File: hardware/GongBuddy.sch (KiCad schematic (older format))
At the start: 49 parts, among them J1 USB_B_Mini, J2 Conn_01x05, J3 2908-05WB-MG, J4 Conn_01x04, J5 Conn_01x02, J6 Conn_01x06, J7 Conn_Coaxial, J8 Conn_01x15, Q1 MMBT3904, U1 TPS7A19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

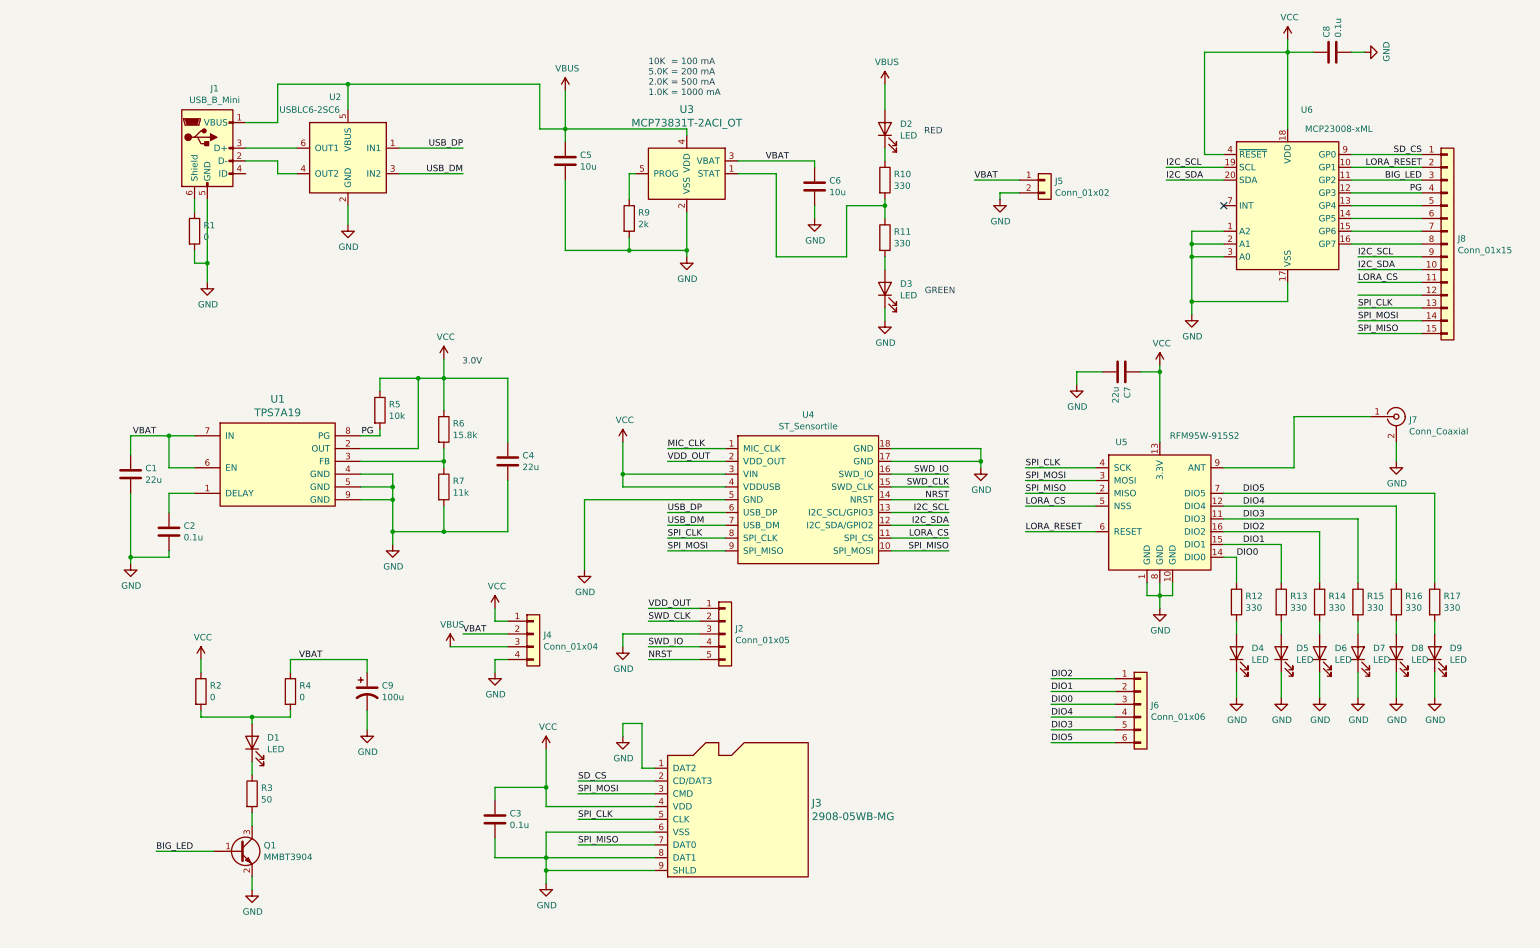
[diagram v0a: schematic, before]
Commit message: Finished the layout and routing.
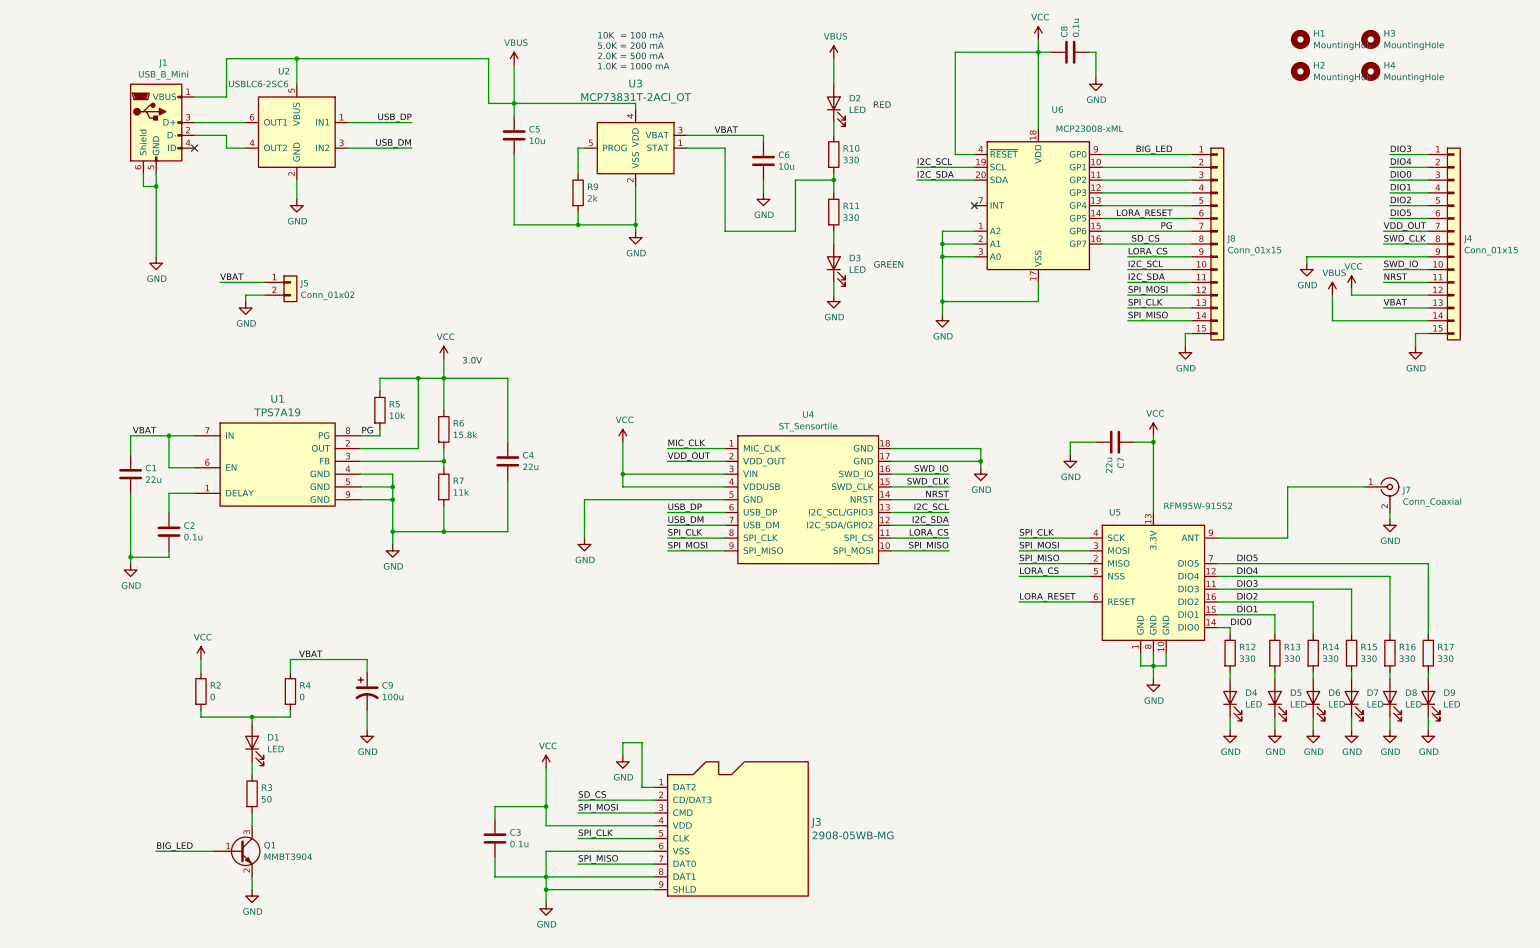
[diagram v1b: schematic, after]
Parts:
- removed J2: Conn_01x05, Connector_PinHeader_2.54mm:PinHeader_1x05_P2.54mm_Vertical, symbol Connector_Generic:Conn_01x05
- removed J4: Conn_01x04, Connector_PinHeader_2.54mm:PinHeader_1x04_P2.54mm_Vertical, symbol Connector_Generic:Conn_01x04
- removed J6: Conn_01x06, Connector_PinHeader_2.54mm:PinHeader_1x06_P2.54mm_Vertical, symbol Connector_Generic:Conn_01x06
- removed R1: 0, Resistor_SMD:R_0603_1608Metric, symbol Device:R
- added H1, H2, H3, H4: MountingHole, MountingHole:MountingHole_2.7mm_M2.5, symbol Mechanical:MountingHole
- added J4: Conn_01x15, Connector_PinHeader_2.54mm:PinHeader_1x15_P2.54mm_Vertical, symbol Connector_Generic:Conn_01x15
- C9: footprint Capacitor_SMD:CP_Elec_6.3x5.7 -> Capacitor_SMD:CP_Elec_3x5.3
- R3: footprint Resistor_SMD:R_0603_1608Metric -> Resistor_SMD:R_1206_3216Metric
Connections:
- net BIG_LED: now also J8.1 (Pin_1), U6.9 (GP0); no longer J8.3 (Pin_3), U6.11 (GP2)
- net DIO0: now also J4.3 (Pin_3)
- net DIO1: now also J4.4 (Pin_4)
- net DIO2: now also J4.5 (Pin_5)
- net DIO3: now also J4.1 (Pin_1)
- net DIO4: now also J4.2 (Pin_2)
- net DIO5: now also J4.6 (Pin_6)
- net GND: now also J1.6 (Shield), J8.15 (Pin_15), J4.15 (Pin_15), J4.9 (Pin_9)
- net I2C_SCL: now also J8.10 (Pin_10); no longer J8.9 (Pin_9)
- net I2C_SDA: now also J8.11 (Pin_11); no longer J8.10 (Pin_10)
- net LORA_CS: now also J8.9 (Pin_9); no longer J8.11 (Pin_11)
- net LORA_RESET: now also J8.6 (Pin_6), U6.14 (GP5); no longer J8.2 (Pin_2), U6.10 (GP1)
- net NRST: now also J4.11 (Pin_11)
- net PG: now also J8.7 (Pin_7), U6.15 (GP6); no longer J8.4 (Pin_4), U6.12 (GP3)
- net SD_CS: now also J8.8 (Pin_8), U6.16 (GP7); no longer J8.1 (Pin_1), U6.9 (GP0)
- net SPI_MISO: now also J8.14 (Pin_14); no longer J8.15 (Pin_15)
- net SPI_MOSI: now also J8.12 (Pin_12); no longer J8.14 (Pin_14)
- net SWD_CLK: now also J4.8 (Pin_8)
- net SWD_IO: now also J4.10 (Pin_10)
- net VBAT: now also J4.13 (Pin_13)
- net VBUS: now also J4.14 (Pin_14)
- net VCC: now also J4.12 (Pin_12)
- net VDD_OUT: now also J4.7 (Pin_7)
- new net: J8.2 (Pin_2), U6.10 (GP1)
- new net: J8.3 (Pin_3), U6.11 (GP2)
- new net: J8.4 (Pin_4), U6.12 (GP3)
- no-connect marks 1 -> 2
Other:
- moved on the sheet: C3, C5, C6, C7, C8, D2, D3, D4, D5, D6, D7, D8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

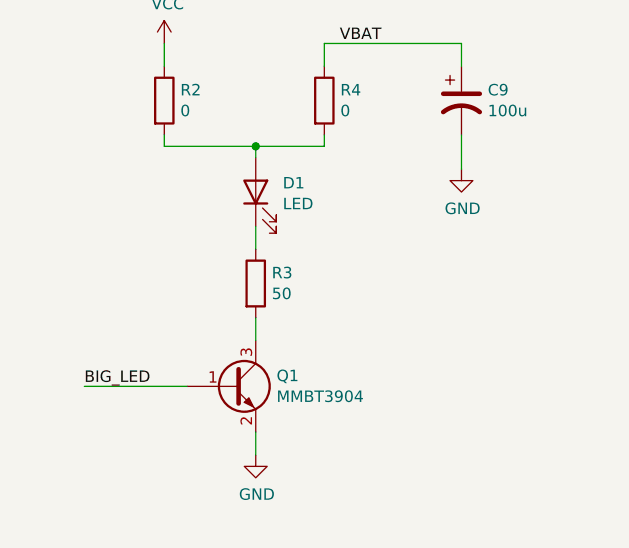
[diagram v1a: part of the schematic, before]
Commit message: Tweaked the layout slightly.
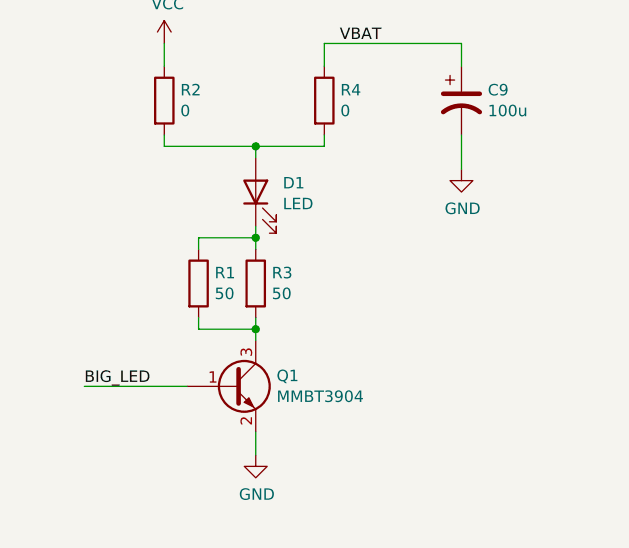
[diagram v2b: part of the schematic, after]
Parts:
- added R1: 50, Resistor_SMD:R_1206_3216Metric, symbol Device:R
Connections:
- net at Q1.3 (C), R3.2: now also R1.2
- net at D1.1 (K), R3.1: now also R1.1
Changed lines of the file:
@@
 VBAT
 Wire Wire Line
-	1600 6400 1600 6500
-Wire Wire Line
-	1600 6800 1600 6900
+	1600 6400 1600 6450
+Wire Wire Line
+	1600 6800 1600 6850
 $Comp
 L power:GND #PWR04
@@
 	850  1900 850  2450
 NoConn ~ 1150 1600
+$Comp
+L Device:R R1
+U 1 1 5F92D8FD
+P 1350 6650
+F 0 "R1" H 1420 6696 50  0000 L CNN
+F 1 "50" H 1420 6605 50  0000 L CNN
+F 2 "Resistor_SMD:R_1206_3216Metric" V 1280 6650 50  0001 C CNN
+F 3 "~" H 1350 6650 50  0001 C CNN
+	1    1350 6650
+	1    0    0    -1
+$EndComp
+Wire Wire Line
+	1350 6500 1350 6450
+Wire Wire Line
+	1350 6450 1600 6450
+Connection ~ 1600 6450
+Wire Wire Line
+	1600 6450 1600 6500
+Wire Wire Line
+	1350 6800 1350 6850
+Wire Wire Line
+	1350 6850 1600 6850
+Connection ~ 1600 6850
+Wire Wire Line
+	1600 6850 1600 6900
 $EndSCHEMATC

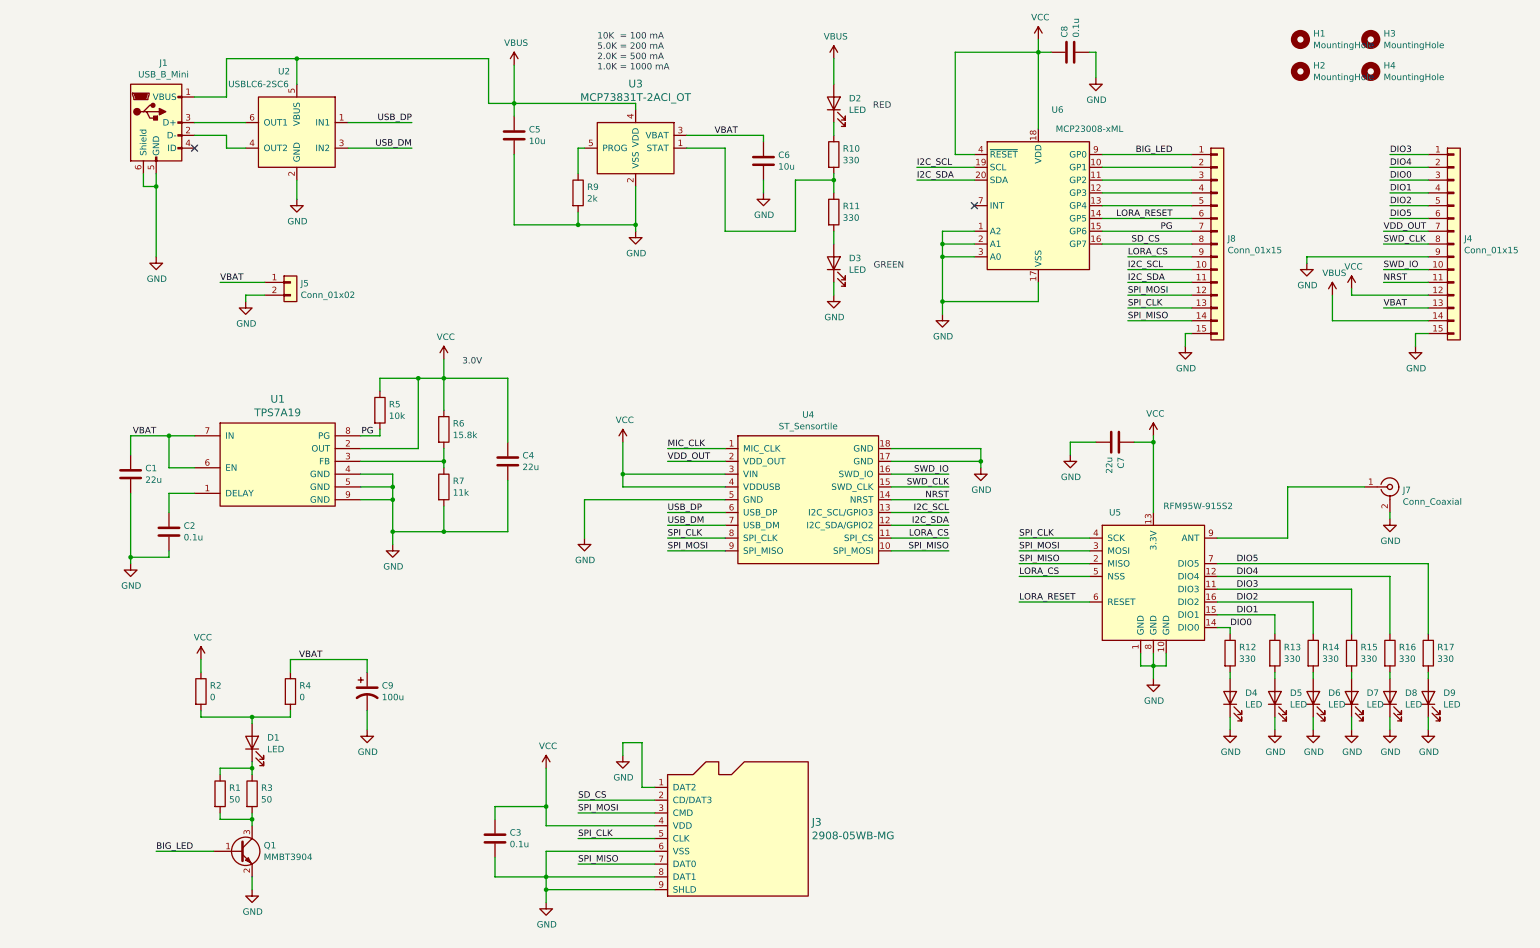
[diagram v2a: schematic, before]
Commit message: Updated the mechanical design, step files, etc.
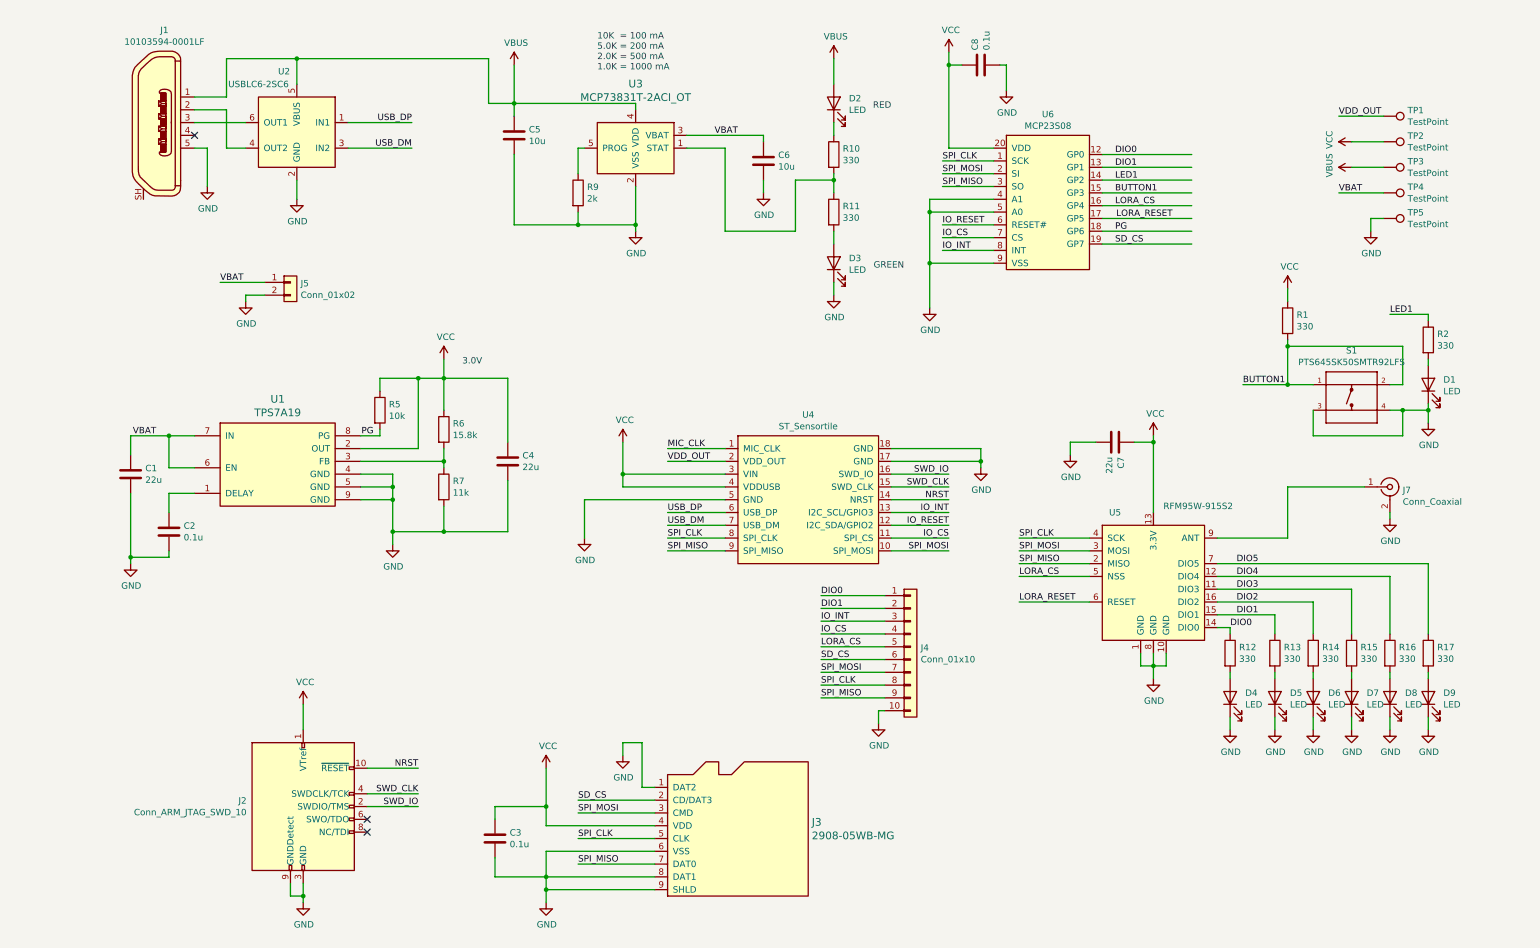
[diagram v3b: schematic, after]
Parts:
- removed C9: 100u, Capacitor_SMD:CP_Elec_3x5.3, symbol Device:CP1
- removed H1, H2, H3, H4: MountingHole, MountingHole:MountingHole_2.7mm_M2.5, symbol Mechanical:MountingHole
- removed J1: USB_B_Mini, Connector_USB:USB_Mini-B_Lumberg_2486_01_Horizontal, symbol Connector:USB_B_Mini
- removed J4, J8: Conn_01x15, Connector_PinHeader_2.54mm:PinHeader_1x15_P2.54mm_Vertical, symbol Connector_Generic:Conn_01x15
- removed Q1: MMBT3904, Package_TO_SOT_SMD:SOT-23, symbol Transistor_BJT:MMBT3904
- removed R3: 50, Resistor_SMD:R_1206_3216Metric, symbol Device:R
- removed R4: 0, Resistor_SMD:R_0603_1608Metric, symbol Device:R
- removed U6: MCP23008-xML, Package_DFN_QFN:QFN-20-1EP_4x4mm_P0.5mm_EP2.7x2.7mm, symbol Interface_Expansion:MCP23008-xML
- added J1: 10103594-0001LF, digikey-footprints:USB_Micro_B_Female_10103594-0001LF, symbol dk_USB-DVI-HDMI-Connectors:10103594-0001LF
- added J2: Conn_ARM_JTAG_SWD_10, KicadFootprint:CortexSWD, symbol Connector:Conn_ARM_JTAG_SWD_10
- added J4: Conn_01x10, Connector_PinHeader_2.54mm:PinHeader_1x10_P2.54mm_Vertical, symbol Connector_Generic:Conn_01x10
- added S1: PTS645SK50SMTR92LFS, mechanical:SW_PTS645SK50SMTR92LFS, symbol PTS645SK50SMTR92LFS:PTS645SK50SMTR92LFS
- added TP1, TP2, TP3, TP4, TP5: TestPoint, TestPoint:TestPoint_Pad_D1.0mm, symbol Connector:TestPoint
- added U6: MCP23S08, Package_SO:SSOP-20_5.3x7.2mm_P0.65mm, symbol General:MCP23S08
- D1: footprint LED_THT:LED_D1.8mm_W1.8mm_H2.4mm_Horizontal_O1.27mm_Z1.6mm -> LED_SMD:LED_0603_1608Metric
- J3: footprint KicadFootprint:AMPHENOL_1140084168 -> digikey-footprints:MicroSD_2908-05WB-MG; Digi-Key_PN 114-00841-68-2-ND -> 3M5607CT-ND; MPN 114-00841-68 -> 2908-05WB-MG
- J7: footprint Connector_Coaxial:SMA_Amphenol_132289_EdgeMount -> KicadFootprint:SAMTEC_SMA-J-P-H-ST-EM1
- R1: value 50 -> 330; footprint Resistor_SMD:R_1206_3216Metric -> Resistor_SMD:R_0603_1608Metric
- R2: value 0 -> 330
- U1: footprint Package_SON:HVSON-8-1EP_3x3mm_P0.65mm_EP1.6x2.4mm -> KicadFootprint:IC_DRV8601DRBT
- U3: footprint Package_TO_SOT_SMD:SOT-23-5 -> digikey-footprints:SOT-753
- U5: footprint RF_Module:HOPERF_RFM9XW_SMD -> KicadFootprint:XCVR_RFM95W-915S2
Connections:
- net labels added: BUTTON1, IO_CS, IO_INT, IO_RESET, LED1
- net labels removed: BIG_LED, I2C_SCL, I2C_SDA
- wire segments 245 -> 238
- no-connect marks 2 -> 3
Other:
- moved on the sheet: C8

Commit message: Added more files.
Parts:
- added TP10, TP11, TP12, TP6, TP7, TP8, TP9: TestPoint, TestPoint:TestPoint_Pad_D1.0mm, symbol Connector:TestPoint
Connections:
- wire segments 238 -> 239
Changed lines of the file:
@@
 $EndComp
 Wire Wire Line
-	5300 3950 4850 3950
+	5300 3950 5200 3950
 Wire Wire Line
 	5300 4150 4500 4150
@@
 	4650 6250 4650 6600
 Text Label 8350 2350 0    50   ~ 0
+LORA_CS
+Text Label 8350 2150 0    50   ~ 0
 SD_CS
-Text Label 8800 2150 2    50   ~ 0
-LORA_RESET
 Text Label 8350 1650 0    50   ~ 0
-DIO0
+PG
 $Comp
 L Device:LED D4
@@
 DIO0
 Text Label 8350 2250 0    50   ~ 0
-PG
+LORA_RESET
 Wire Wire Line
 	10450 1350 10100 1350
@@
 SPI_MISO
 Text Label 6050 5700 0    50   ~ 0
+SPI_CLK
+Text Label 6050 5800 0    50   ~ 0
 SPI_MOSI
-Text Label 6050 5800 0    50   ~ 0
-SPI_CLK
 Wire Wire Line
 	6550 5900 6050 5900
@@
 IO_RESET
 Text Label 8350 2050 0    50   ~ 0
-LORA_CS
+BUTTON1
 Text Label 8350 1750 0    50   ~ 0
+DIO0
+Text Label 8350 1850 0    50   ~ 0
 DIO1
-Text Label 8350 1850 0    50   ~ 0
+Text Label 8350 1950 0    50   ~ 0
 LED1
-Text Label 8350 1950 0    50   ~ 0
-BUTTON1
 $Comp
 L dk_USB-DVI-HDMI-Connectors:10103594-0001LF J1
@@
 Text Label 6050 5200 0    50   ~ 0
 DIO1
+$Comp
+L Connector:TestPoint TP11
+U 1 1 6098CF77
+P 10800 2900
+F 0 "TP11" V 10754 3088 50  0000 L CNN
+F 1 "TestPoint" V 10845 3088 50  0000 L CNN
+F 2 "TestPoint:TestPoint_Pad_D1.0mm" H 11000 2900 50  0001 C CNN
+F 3 "~" H 11000 2900 50  0001 C CNN
+	1    10800 2900
+	0    1    1    0
+$EndComp
+Connection ~ 10800 2900
+$Comp
+L Connector:TestPoint TP7
+U 1 1 6098D620
+P 9700 3450
+F 0 "TP7" V 9654 3638 50  0000 L CNN
+F 1 "TestPoint" V 9745 3638 50  0000 L CNN
+F 2 "TestPoint:TestPoint_Pad_D1.0mm" H 9900 3450 50  0001 C CNN
+F 3 "~" H 9900 3450 50  0001 C CNN
+	1    9700 3450
+	-1   0    0    1
+$EndComp
+$Comp
+L Connector:TestPoint TP12
+U 1 1 6098E6DE
+P 10800 4850
+F 0 "TP12" V 10754 5038 50  0000 L CNN
+F 1 "TestPoint" V 10845 5038 50  0000 L CNN
+F 2 "TestPoint:TestPoint_Pad_D1.0mm" H 11000 4850 50  0001 C CNN
+F 3 "~" H 11000 4850 50  0001 C CNN
+	1    10800 4850
+	0    1    1    0
+$EndComp
+Connection ~ 10800 4850
+$Comp
+L Connector:TestPoint TP10
+U 1 1 6098F2FA
+P 10500 4950
+F 0 "TP10" V 10454 5138 50  0000 L CNN
+F 1 "TestPoint" V 10545 5138 50  0000 L CNN
+F 2 "TestPoint:TestPoint_Pad_D1.0mm" H 10700 4950 50  0001 C CNN
+F 3 "~" H 10700 4950 50  0001 C CNN
+	1    10500 4950
+	0    1    1    0
+$EndComp
+Connection ~ 10500 4950
+$Comp
+L Connector:TestPoint TP9
+U 1 1 6098F5E5
+P 10200 5050
+F 0 "TP9" V 10154 5238 50  0000 L CNN
+F 1 "TestPoint" V 10245 5238 50  0000 L CNN
+F 2 "TestPoint:TestPoint_Pad_D1.0mm" H 10400 5050 50  0001 C CNN
+F 3 "~" H 10400 5050 50  0001 C CNN
+	1    10200 5050
+	0    1    1    0
+$EndComp
+Connection ~ 10200 5050
+$Comp
+L Connector:TestPoint TP8
+U 1 1 6098F91E
+P 9900 5150
+F 0 "TP8" V 9854 5338 50  0000 L CNN
+F 1 "TestPoint" V 9945 5338 50  0000 L CNN
+F 2 "TestPoint:TestPoint_Pad_D1.0mm" H 10100 5150 50  0001 C CNN
+F 3 "~" H 10100 5150 50  0001 C CNN
+	1    9900 5150
+	0    1    1    0
+$EndComp
+Connection ~ 9900 5150
+$Comp
+L Connector:TestPoint TP6
+U 1 1 6098FB91
+P 5200 3950
+F 0 "TP6" V 5154 4138 50  0000 L CNN
+F 1 "TestPoint" V 5245 4138 50  0000 L CNN
+F 2 "TestPoint:TestPoint_Pad_D1.0mm" H 5400 3950 50  0001 C CNN
+F 3 "~" H 5400 3950 50  0001 C CNN
+	1    5200 3950
+	1    0    0    -1
+$EndComp
+Connection ~ 5200 3950
+Wire Wire Line
+	5200 3950 4850 3950
 $EndSCHEMATC
